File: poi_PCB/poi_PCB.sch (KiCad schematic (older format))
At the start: 69 parts, among them J4 USB_C_Receptacle_USB2.0, Q1 AO4407C, Q2 AO3400A, Q3 AO3400A, Q4 AO3400A, Q5 AO4407C, SW3 TL2233OA, U1 ESP32-WROOM-32D, U2 CH340C, U3 AMS1117-3.3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

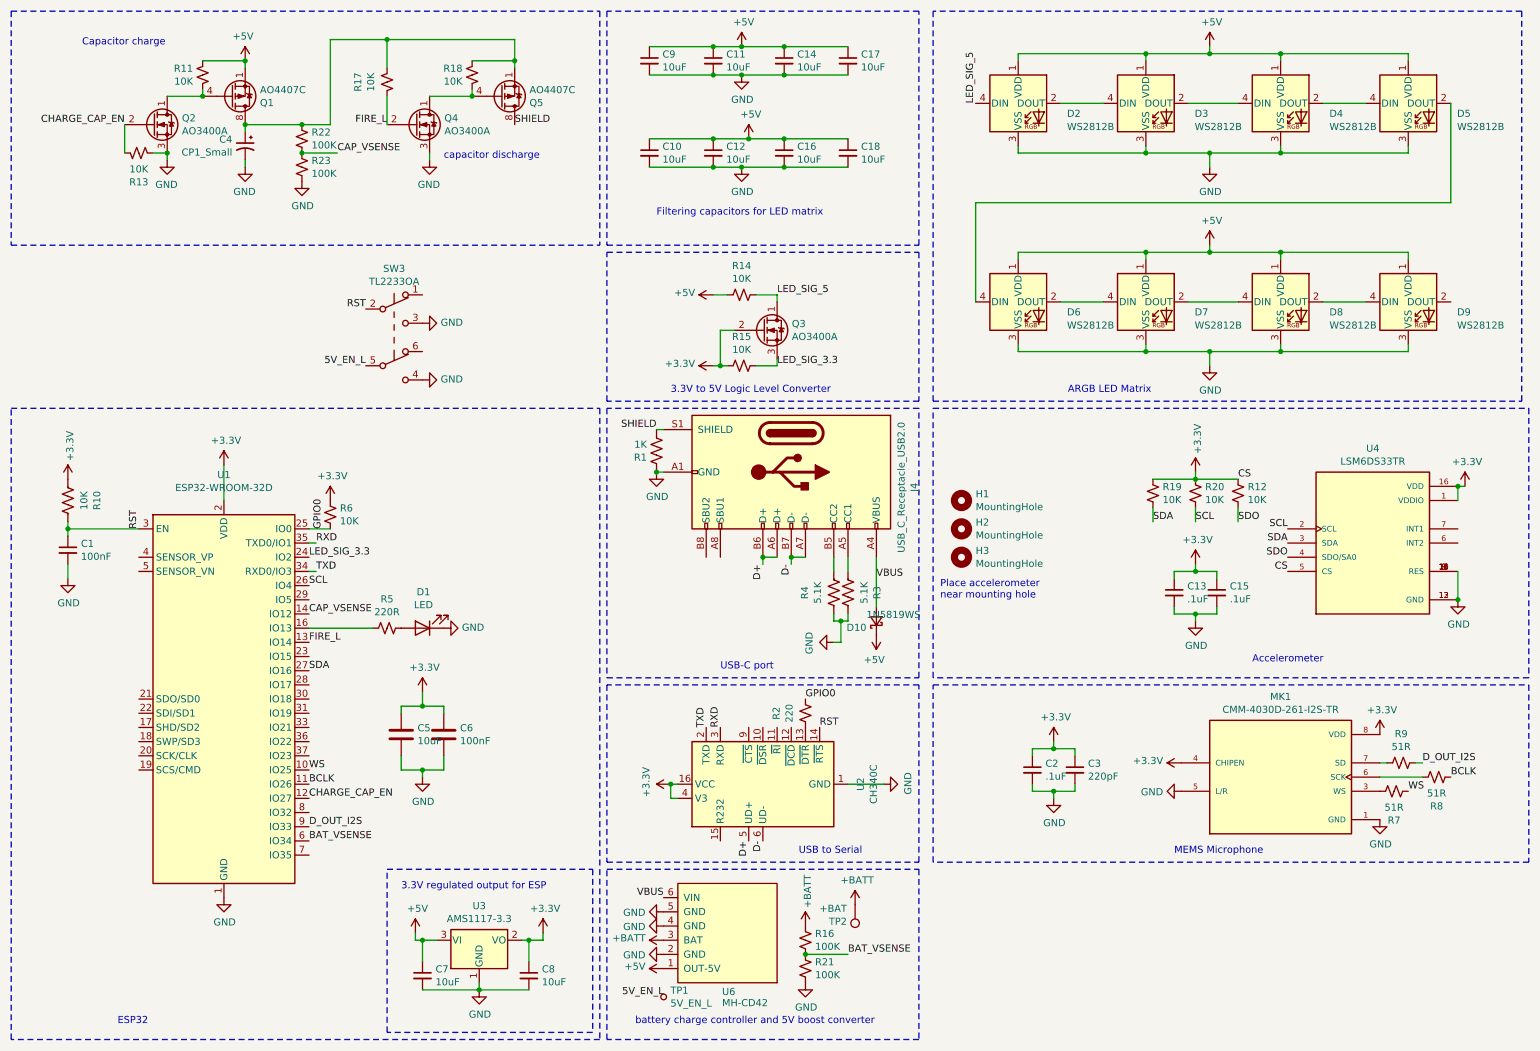
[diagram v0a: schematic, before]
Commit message: Updated pictures and schematics, added analog RGB header
analog RGB header is designed for 12V analog RGB strips
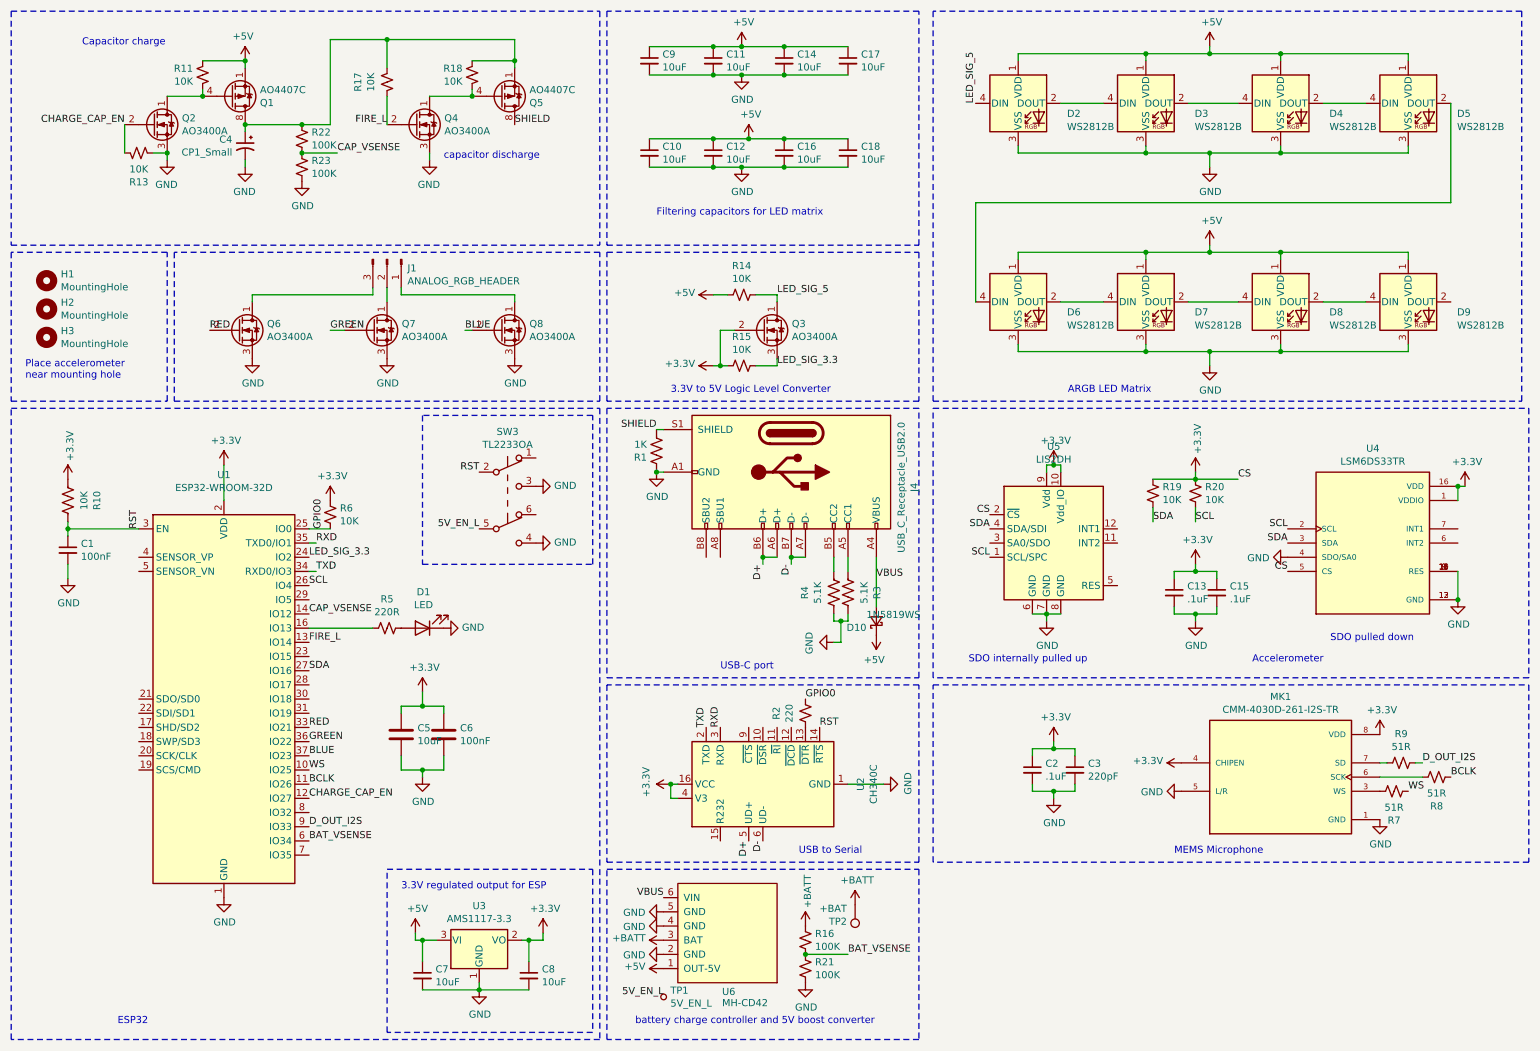
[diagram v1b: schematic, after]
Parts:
- removed R12: 10K, Resistor_SMD:R_0402_1005Metric, symbol Device:R_Small_US
- added J1: ANALOG_RGB_HEADER, Connector_PinHeader_2.54mm:PinHeader_1x03_P2.54mm_Vertical, symbol Connector:Conn_01x03_Male
- added Q6, Q7, Q8: AO3400A, Package_TO_SOT_SMD:SOT-23, symbol Device:Q_NMOS_DGS
- added U5: LIS2DH, Package_LGA:LGA-12_2x2mm_P0.5mm, symbol Sensor_Motion:LIS2HH12
- D2, D3, D4, D5, D6, D7, D8, D9: LCSC C139127 -> (none); MANUFACTURER (none) -> Aliexpress
- H1, H2, H3, TP1, TP2: MANUFACTURER (none) -> NA
- J4, SW3: MANUFACTURER (none) -> Digikey
- MK1: MANUFACTURER CUI Devices -> Local
- U1, U6: MANUFACTURER (none) -> Local
- U2: MANUFACTURER (none) -> Aliexpress
- U3: LCSC C6186 -> (none); MANUFACTURER (none) -> Local
- U4: MANUFACTURER STMicroelectronics -> Local
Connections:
- net SDO is gone; now on net GND: U4.4 (SDO/SA0)
- net +3V3: now also U5.10 (Vdd_IO), U5.2 (~CS), U5.9 (Vdd)
- net GND: now also Q6.3 (S), Q7.3 (S), Q8.3 (S), U5.6 (GND), U5.7 (GND), U5.8 (GND)
- net SCL: now also U5.1 (SCL/SPC)
- net SDA: now also U5.4 (SDA/SDI)
- net RED: now reaches U1.33 (IO21)
- net RED: now also Q6.2 (G)
- net GREEN: now reaches U1.36 (IO22)
- net GREEN: now also Q7.2 (G)
- net BLUE: now reaches U1.37 (IO23)
- net BLUE: now also Q8.2 (G)
- new net: J1.3 (Pin_3), Q6.1 (D)
- new net: J1.2 (Pin_2), Q7.1 (D)
- new net: J1.1 (Pin_1), Q8.1 (D)
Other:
- note added: "SDO internally pulled up\n"
- note added: "SDO pulled down\n"
- moved on the sheet: H1, H2, H3, SW3

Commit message: Added fabrication files
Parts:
- C4: value CP1_Small -> 0.47F
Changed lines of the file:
@@
 P 2150 1450
 F 0 "C4" H 2241 1496 50  0000 L CNN
-F 1 "CP1_Small" H 2241 1405 50  0000 L CNN
+F 1 "0.47F" H 2241 1405 50  0000 L CNN
 F 2 "Capacitor_THT:CP_Radial_D13.0mm_P5.00mm" H 2150 1450 50  0001 C CNN
 F 3 "~" H 2150 1450 50  0001 C CNN

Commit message: Changed schematic based on testing
-LED logic level shifter omitted due to slow switching speed of AO3400A
-LED input moved to GPIO5 to avoid pulling up GPIO2 during UART programming
-Gate pullup/pulldown resistors changed to 1K to allow for faster switching
-analog RGB header omitted
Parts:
- removed J1: ANALOG_RGB_HEADER, Connector_PinHeader_2.54mm:PinHeader_1x03_P2.54mm_Vertical, symbol Connector:Conn_01x03_Male
- removed Q2, Q3, Q4, Q6, Q7, Q8: AO3400A, Package_TO_SOT_SMD:SOT-23, symbol Device:Q_NMOS_DGS
- removed R14, R15: 10K, Resistor_SMD:R_0603_1608Metric, symbol Device:R_Small_US
- added Q2, Q6: AO3400A, Package_TO_SOT_SMD:SOT-23, symbol Device:Q_NMOS_SGD
- R11, R13, R17, R18: value 10K -> 1K
- renumbered TP2 to +BAT, TP1 to EN_L
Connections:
- net LED_SIG_5 is gone; now on net LED_SIG: D2.4 (DIN)
- net CHARGE_CAP_EN: now also Q2.2 (G)
- net FIRE_L: now also Q6.2 (G)
- net GND: now also Q2.1 (S), Q6.1 (S)
- net LED_SIG: now reaches U1.29 (IO5)
- net at Q1.4 (G), R11.2: now also Q2.3 (D)
- net at Q5.4 (G), R18.2: now also Q6.3 (D)
- net BLUE: no longer names the net of U1.37 (IO23)
- net GREEN: no longer names the net of U1.36 (IO22)
- net LED_SIG_3.3: no longer names the net of U1.24 (IO2)
- net RED: no longer names the net of U1.33 (IO21)
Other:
- note added: "ON/RESET BUTTON"
- note removed: "3.3V to 5V Logic Level Converter\n"
- moved on the sheet: +BAT, C7, C8, SW3, U3

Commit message: Update poi_PCB.sch
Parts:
- SW3: LCSC (none) -> C692487
- U2: LCSC (none) -> C84681
- U5: LCSC (none) -> C110926
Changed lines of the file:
@@
 F 3 "https://datasheet.lcsc.com/szlcsc/Jiangsu-Qin-Heng-CH340C_C84681.pdf" H 5450 6750 50  0001 C CNN
 F 4 "Aliexpress" H 5800 5950 50  0001 C CNN "MANUFACTURER"
+F 5 "C84681" H 5800 5950 50  0001 C CNN "LCSC"
 	1    5800 5950
 	0    -1   -1   0
@@
 F 3 "~" H 2250 3050 50  0001 C CNN
 F 4 "Digikey" H 2250 2850 50  0001 C CNN "MANUFACTURER"
+F 5 "C692487" H 2250 2850 50  0001 C CNN "LCSC"
 	1    2250 2850
 	1    0    0    -1
@@
 F 3 "http://www.st.com/web/en/resource/technical/document/datasheet/DM00042751.pdf" H 7450 4250 50  0001 C CNN
 F 4 "C110926" H 7800 4250 50  0001 C CNN "MANUFACTURER"
+F 5 "C110926" H 7800 4250 50  0001 C CNN "LCSC"
 	1    7800 4250
 	1    0    0    -1
